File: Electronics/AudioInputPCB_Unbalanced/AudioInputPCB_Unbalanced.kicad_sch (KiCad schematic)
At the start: 109 parts, among them J1 IDC Header, J2 RCA x2, J3 RCA x2, J4 RCA x2, J5 RCA x2, U1 NE5532, U2 NE5532, U3 NE5532, U4 NE5532

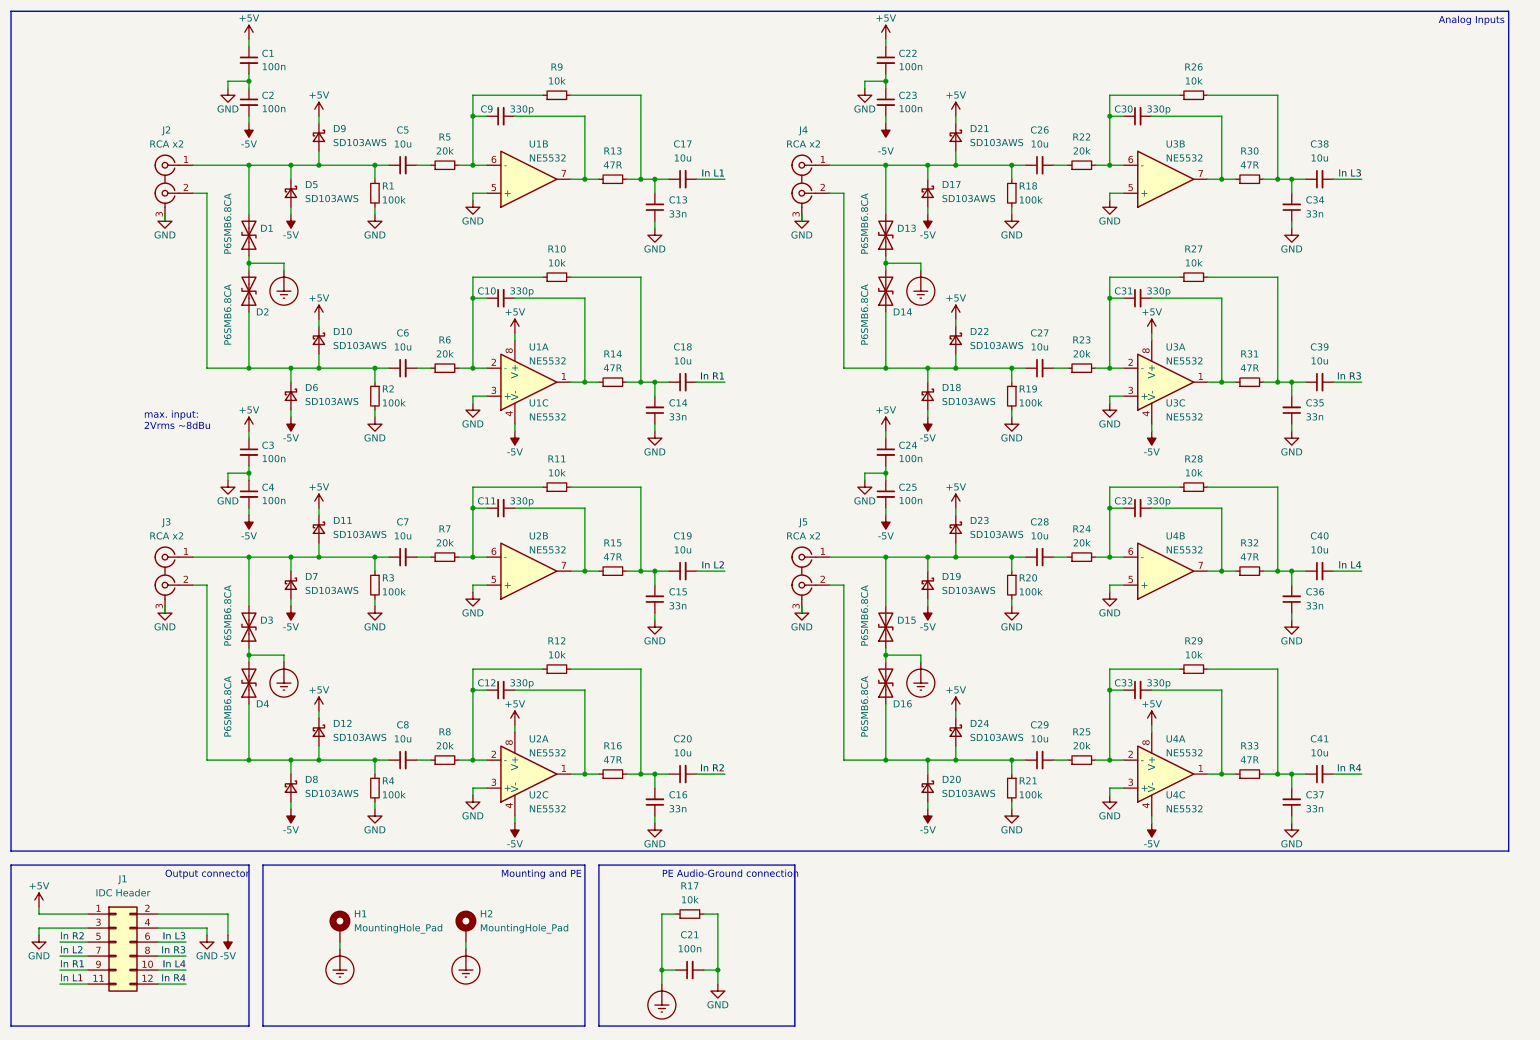
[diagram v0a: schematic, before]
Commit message: Finishes SmallDSP Maxi plus the fitting In- and Output Boards
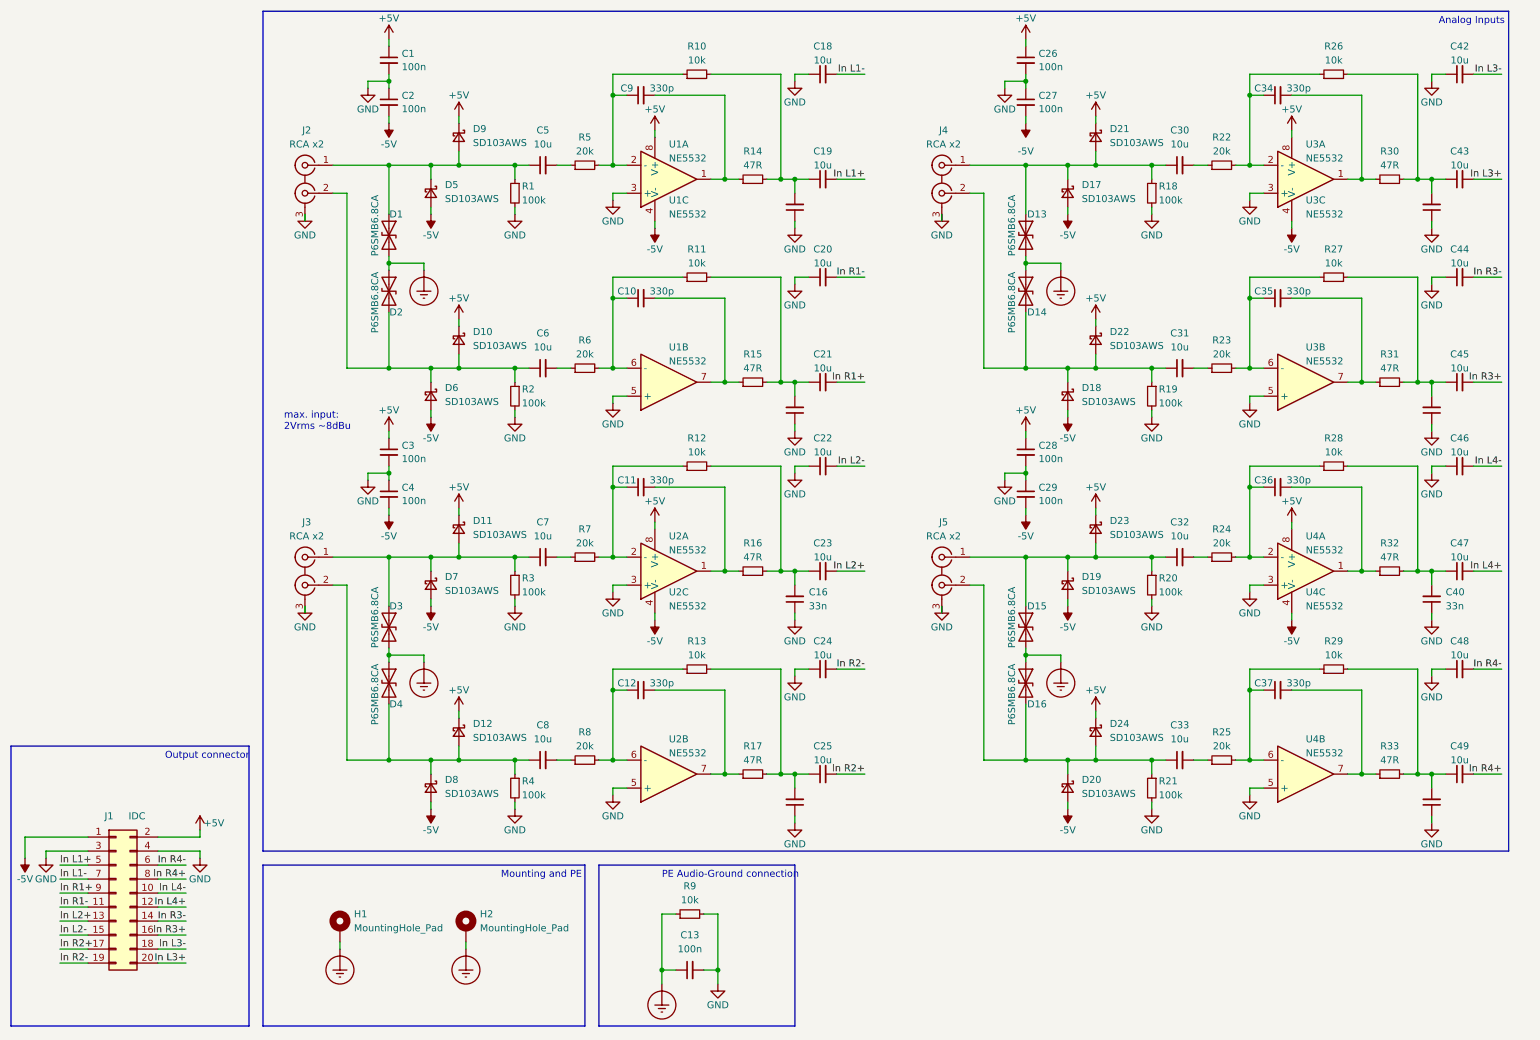
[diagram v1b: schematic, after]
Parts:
- removed C17, C38, C39, C40, C41: 10u, Capacitor_SMD:C_1206_3216Metric, symbol Device:C_Small
- removed J1: IDC Header, Connector_IDC:IDC-Header_2x06_P2.54mm_Vertical, symbol Connector_Generic:Conn_02x06_Odd_Even
- added C21, C22, C23, C24, C25, C42, C43, C44, C45, C46, C47, C48, C49: 10u, Capacitor_SMD:C_1206_3216Metric, symbol Device:C_Small
- added J1: IDC, Connector_IDC:IDC-Header_2x10_P2.54mm_Vertical, symbol Connector_Generic:Conn_02x10_Odd_Even
- renumbered C9 to C10, C12 to C11, C11 to C12, C21 to C13, C13 to C15, C15 to C17, C22 to C26, C23 to C27, C24 to C28, C25 to C29, C27 to C30, C26 to C31, C29 to C32, C28 to C33, C31 to C34, C30 to C35, C33 to C36, C32 to C37, C35 to C38, C34 to C39, C37 to C40, C36 to C41, C6 to C5, C5 to C6, C8 to C7, C7 to C8, C10 to C9, D2 to D1, D9 to D10, D12 to D11, D11 to D12, D14 to D13, D13 to D14, D16 to D15, D15 to D16, D18 to D17, D17 to D18, D20 to D19, D1 to D2, D19 to D20, D22 to D21, D21 to D22, D24 to D23, D23 to D24, D4 to D3, D3 to D4, D6 to D5, D5 to D6, D8 to D7, D7 to D8, D10 to D9, R2 to R1, R9 to R11, R11 to R13, R13 to R15, R15 to R17, R19 to R18, R18 to R19, R1 to R2, R21 to R20, R20 to R21, R23 to R22, R22 to R23, R25 to R24, R24 to R25, R27 to R26, R26 to R27, R29 to R28, R28 to R29, R4 to R3, R31 to R30, R30 to R31, R33 to R32, R32 to R33, R3 to R4, R6 to R5, R5 to R6, R8 to R7, R7 to R8, R17 to R9
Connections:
- net +5V: now also J1.2 (Pin_2)
- net -5V: now also J1.1 (Pin_1)
- net GND: now also C18.1, C20.1, C22.1, C24.1, C42.1, C44.1, C46.1, C48.1, J1.3 (Pin_3), J1.4 (Pin_4)
- net at C30.1, D13.1 (A1), D17.1 (K)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: now also J4.1 (IN1); no longer J4.2 (IN2)
- net at C8.1, D12.2 (A), D4.2 (A2)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: now also J3.2 (IN2); no longer J3.1 (IN1)
- net at C7.1, D11.2 (A), D3.1 (A1)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: now also J3.1 (IN1); no longer J3.2 (IN2)
- net at C17.2, R13.2, R17.2: now also C25.1; no longer C19.1
- net at C38.2, R26.2, R30.2: now also C43.1
- net at C6.1, D10.2 (A), D2.2 (A2)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: now also J2.2 (IN2); no longer J2.1 (IN1)
- net at C5.1, D1.1 (A1), D5.1 (K)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: now also J2.1 (IN1); no longer J2.2 (IN2)
- net at C15.2, R11.2, R15.2: now also C21.1
- net at C32.1, D15.1 (A1), D19.1 (K)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: now also J5.1 (IN1); no longer J5.2 (IN2)
- net at C33.1, D16.2 (A2), D20.1 (K)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: now also J5.2 (IN2); no longer J5.1 (IN1)
- net at C31.1, D14.2 (A2), D18.1 (K)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: now also J4.2 (IN2); no longer J4.1 (IN1)
- net at C39.2, R27.2, R31.2: now also C45.1
- net at C41.2, R29.2, R33.2: now also C49.1
- net at C16.2, R12.2, R16.2: now also C23.1; no longer C20.1
- net at C14.2, R10.2, R14.2: now also C19.1; no longer C18.1
- net at C40.2, R28.2, R32.2: now also C47.1
- net In L2 renamed In L1+
- net In L1+: now also J1.5 (Pin_5)
- net In R1 renamed In L1-
- net In L1-: now also J1.7 (Pin_7)
- net In R2 renamed In R1-
- net In R1-: now also J1.11 (Pin_11)
- new net In L2+: C23.2, J1.13 (Pin_13)
- new net In L2-: C22.2, J1.15 (Pin_15)
- new net In L3+: C43.2, J1.20 (Pin_20)
- new net In L3-: C42.2, J1.18 (Pin_18)
- new net In L4+: C47.2, J1.12 (Pin_12)
- new net In L4-: C46.2, J1.10 (Pin_10)
- new net In R1+: C21.2, J1.9 (Pin_9)
- new net In R2+: C25.2, J1.17 (Pin_17)
- new net In R2-: C24.2, J1.19 (Pin_19)
- new net In R3+: C45.2, J1.16 (Pin_16)
- new net In R3-: C44.2, J1.14 (Pin_14)
- new net In R4+: C49.2, J1.8 (Pin_8)
- new net In R4-: C48.2, J1.6 (Pin_6)
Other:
- moved on the sheet: C1, C10, C11, C12, C16, C2, C26, C27, C28, C29, C3, C30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

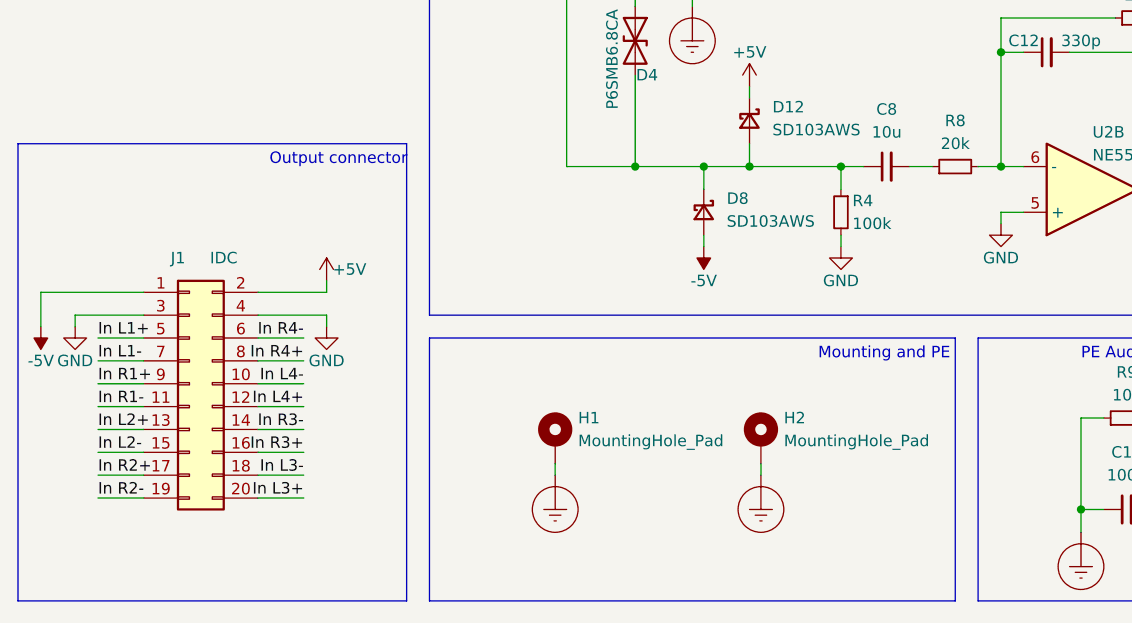
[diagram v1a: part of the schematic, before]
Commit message: adds usb to i2s bridge to micro. Adds tweaks for layout of maxi.
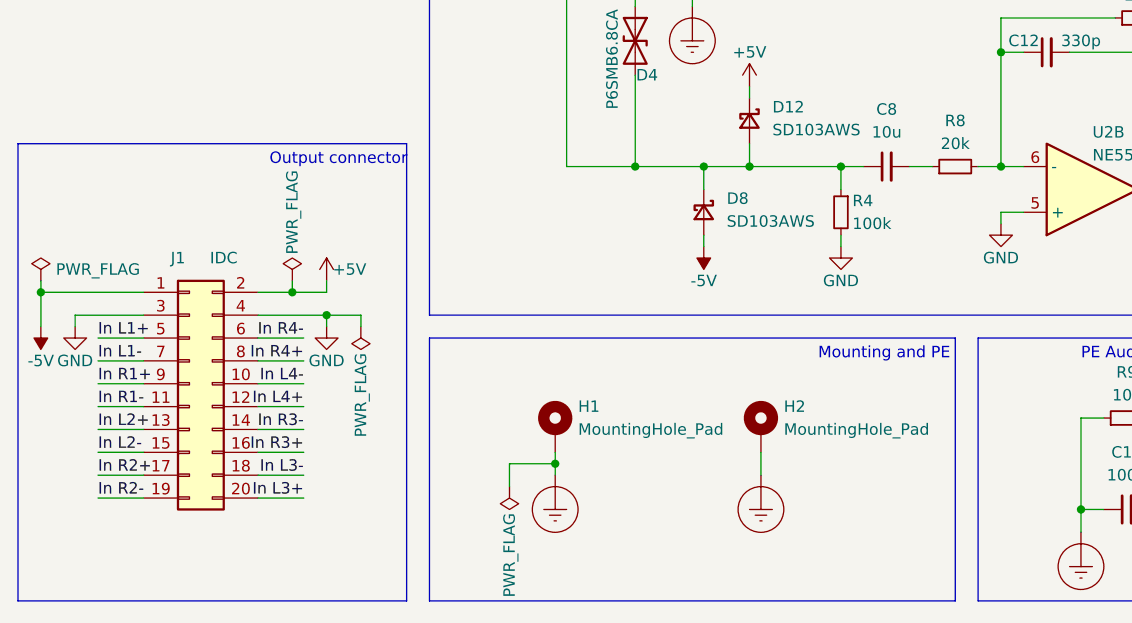
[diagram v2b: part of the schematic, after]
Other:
- moved on the sheet: H1, H2
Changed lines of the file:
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@@
   (title_block
     (title "Unbalanced Analog Input Board for SmallDSP")
-    (date "2023-10-23")
+    (date "2023-11-06")
     (rev "1.0")
     (company "Till Heuer")
@@
   (junction (at 81.28 111.76) (diameter 0) (color 0 0 0 0)
   )
+  (junction (at 15.24 162.56) (diameter 0) (color 0 0 0 0)
+  )
   (junction (at 142.24 151.13) (diameter 0) (color 0 0 0 0)
   )
@@
   (junction (at 237.49 77.47) (diameter 0) (color 0 0 0 0)
   )
+  (junction (at 46.99 165.1) (diameter 0) (color 0 0 0 0)
+  )
   (junction (at 204.47 111.76) (diameter 0) (color 0 0 0 0)
   )
   (junction (at 257.81 151.13) (diameter 0) (color 0 0 0 0)
   )
+  (junction (at 72.39 181.61) (diameter 0) (color 0 0 0 0)
+  )
   (junction (at 81.28 25.4) (diameter 0) (color 0 0 0 0)
   )
@@
   (junction (at 219.71 148.59) (diameter 0) (color 0 0 0 0)
   )
+  (junction (at 43.18 162.56) (diameter 0) (color 0 0 0 0)
+  )
   (junction (at 196.85 40.64) (diameter 0) (color 0 0 0 0)
   )
@@
     (stroke (width 0) (type default))
   )
+  (wire (pts (xy 43.18 162.56) (xy 46.99 162.56))
+    (stroke (width 0) (type default))
+  )
   (wire (pts (xy 152.4 80.01) (xy 149.86 80.01))
     (stroke (width 0) (type default))
@@
     (stroke (width 0) (type default))
   )
+  (wire (pts (xy 67.31 181.61) (xy 72.39 181.61))
+    (stroke (width 0) (type default))
+  )
   (polyline (pts (xy 116.84 167.64) (xy 116.84 196.85))
     (stroke (width 0) (type default))
@@
     (stroke (width 0) (type default))
   )
+  (wire (pts (xy 15.24 161.29) (xy 15.24 162.56))
+    (stroke (width 0) (type default))
+  )
   (wire (pts (xy 257.81 43.18) (xy 255.27 43.18))
     (stroke (width 0) (type default))
@@
     (stroke (width 0) (type default))
   )
+  (wire (pts (xy 72.39 180.34) (xy 72.39 181.61))
+    (stroke (width 0) (type default))
+  )
   (wire (pts (xy 154.94 80.01) (xy 152.4 80.01))
     (stroke (width 0) (type default))
@@
     (stroke (width 0) (type default))
   )
-  (wire (pts (xy 95.25 181.61) (xy 95.25 182.88))
+  (wire (pts (xy 95.25 180.34) (xy 95.25 182.88))
     (stroke (width 0) (type default))
   )
@@
     (stroke (width 0) (type default))
   )
+  (wire (pts (xy 50.8 166.37) (xy 50.8 165.1))
+    (stroke (width 0) (type default))
+  )
   (wire (pts (xy 119.38 111.76) (xy 121.92 111.76))
     (stroke (width 0) (type default))
@@
     (stroke (width 0) (type default))
   )
+  (wire (pts (xy 50.8 165.1) (xy 46.99 165.1))
+    (stroke (width 0) (type default))
+  )
   (wire (pts (xy 154.94 50.8) (xy 154.94 52.07))
     (stroke (width 0) (type default))
@@
     (stroke (width 0) (type default))
   )
-  (wire (pts (xy 39.37 162.56) (xy 46.99 162.56))
+  (wire (pts (xy 39.37 162.56) (xy 43.18 162.56))
     (stroke (width 0) (type default))
   )
@@
     (stroke (width 0) (type default))
   )
+  (wire (pts (xy 43.18 161.29) (xy 43.18 162.56))
+    (stroke (width 0) (type default))
+  )
   (wire (pts (xy 245.11 135.89) (xy 257.81 135.89))
     (stroke (width 0) (type default))
@@
     (stroke (width 0) (type default))
   )
+  (wire (pts (xy 67.31 184.15) (xy 67.31 181.61))
+    (stroke (width 0) (type default))
+  )
   (wire (pts (xy 88.9 85.09) (xy 88.9 86.36))
     (stroke (width 0) (type default))
@@
     )
   )
-  (symbol (lib_id "Mechanical:MountingHole_Pad") (at 72.39 179.07 0) (unit 1)
+  (symbol (lib_id "Mechanical:MountingHole_Pad") (at 72.39 177.8 0) (unit 1)
     (in_bom yes) (on_board yes) (dnp no) (fields_autoplaced)
-    (property "Reference" "H1" (at 74.93 176.5299 0)
+    (property "Reference" "H1" (at 74.93 175.2599 0)
       (effects (font (size 1.27 1.27)) (justify left))
     )
-    (property "Value" "MountingHole_Pad" (at 74.93 179.0699 0)
+    (property "Value" "MountingHole_Pad" (at 74.93 177.7999 0)
       (effects (font (size 1.27 1.27)) (justify left))
     )
-    (property "Footprint" "MountingHole:MountingHole_3.2mm_M3_Pad_Via" (at 72.39 179.07 0)
+    (property "Footprint" "MountingHole:MountingHole_3.2mm_M3_Pad_Via" (at 72.39 177.8 0)
       (effects (font (size 1.27 1.27)) hide)
     )
-    (property "Datasheet" "~" (at 72.39 179.07 0)
+    (property "Datasheet" "~" (at 72.39 177.8 0)
       (effects (font (size 1.27 1.27)) hide)
     )
-    (property "Manufacturer" "-" (at 72.39 179.07 0)
+    (property "Manufacturer" "-" (at 72.39 177.8 0)
       (effects (font (size 1.27 1.27)) hide)
     )
-    (property "Part Number" "-" (at 72.39 179.07 0)
+    (property "Part Number" "-" (at 72.39 177.8 0)
       (effects (font (size 1.27 1.27)) hide)
     )
-    (property "LCSC Part #" "-" (at 72.39 179.07 0)
+    (property "LCSC Part #" "-" (at 72.39 177.8 0)
       (effects (font (size 1.27 1.27)) hide)
     )
@@
     )
   )
+  (symbol (lib_id "power:PWR_FLAG") (at 43.18 161.29 0) (unit 1)
+    (in_bom yes) (on_board yes) (dnp no)
+    (property "Reference" "#FLG02" (at 43.18 159.385 0)
+      (effects (font (size 1.27 1.27)) hide)
+    )
+    (property "Value" "PWR_FLAG" (at 43.18 153.67 90)
+      (effects (font (size 1.27 1.27)))
+    )
+    (property "Footprint" "" (at 43.18 161.29 0)
+      (effects (font (size 1.27 1.27)) hide)
+    )
+    (property "Datasheet" "~" (at 43.18 161.29 0)
+      (effects (font (size 1.27 1.27)) hide)
+    )
+    (pin "1")
+    (instances
+      (project "AudioInputPCB_Unbalanced"
+        (path "/17188c6f-f81f-4113-81fa-be4890d4152c"
+          (reference "#FLG02") (unit 1)
+        )
+      )
+    )
+  )
   (symbol (lib_id "power:GND") (at 193.04 97.79 0) (unit 1)
     (in_bom yes) (on_board yes) (dnp no)
@@
     )
   )
+  (symbol (lib_id "power:PWR_FLAG") (at 15.24 161.29 0) (unit 1)
+    (in_bom yes) (on_board yes) (dnp no)
+    (property "Reference" "#FLG01" (at 15.24 159.385 0)
+      (effects (font (size 1.27 1.27)) hide)
+    )
+    (property "Value" "PWR_FLAG" (at 21.59 160.02 0)
+      (effects (font (size 1.27 1.27)))
+    )
+    (property "Footprint" "" (at 15.24 161.29 0)
+      (effects (font (size 1.27 1.27)) hide)
+    )
+    (property "Datasheet" "~" (at 15.24 161.29 0)
+      (effects (font (size 1.27 1.27)) hide)
+    )
+    (pin "1")
+    (instances
+      (project "AudioInputPCB_Unbalanced"
+        (path "/17188c6f-f81f-4113-81fa-be4890d4152c"
+          (reference "#FLG01") (unit 1)
+        )
+      )
+    )
+  )
   (symbol (lib_id "Connector:Conn_Coaxial_x2") (at 181.61 114.3 0) (mirror y) (unit 1)
     (in_bom yes) (on_board yes) (dnp no)
@@
     )
   )
+  (symbol (lib_id "power:PWR_FLAG") (at 50.8 166.37 180) (unit 1)
+    (in_bom yes) (on_board yes) (dnp no)
+    (property "Reference" "#FLG03" (at 50.8 168.275 0)
+      (effects (font (size 1.27 1.27)) hide)
+    )
+    (property "Value" "PWR_FLAG" (at 50.8 173.99 90)
+      (effects (font (size 1.27 1.27)))
+    )
+    (property "Footprint" "" (at 50.8 166.37 0)
+      (effects (font (size 1.27 1.27)) hide)
+    )
+    (property "Datasheet" "~" (at 50.8 166.37 0)
+      (effects (font (size 1.27 1.27)) hide)
+    )
+    (pin "1")
+    (instances
+      (project "AudioInputPCB_Unbalanced"
+        (path "/17188c6f-f81f-4113-81fa-be4890d4152c"
+          (reference "#FLG03") (unit 1)
+        )
+      )
+    )
+  )
   (symbol (lib_id "power:GND") (at 140.97 189.23 0) (unit 1)
     (in_bom yes) (on_board yes) (dnp no)
@@
     )
   )
-  (symbol (lib_id "Mechanical:MountingHole_Pad") (at 95.25 179.07 0) (unit 1)
+  (symbol (lib_id "Mechanical:MountingHole_Pad") (at 95.25 177.8 0) (unit 1)
     (in_bom yes) (on_board yes) (dnp no) (fields_autoplaced)
-    (property "Reference" "H2" (at 97.79 176.5299 0)
+    (property "Reference" "H2" (at 97.79 175.2599 0)
       (effects (font (size 1.27 1.27)) (justify left))
     )
-    (property "Value" "MountingHole_Pad" (at 97.79 179.0699 0)
+    (property "Value" "MountingHole_Pad" (at 97.79 177.7999 0)
       (effects (font (size 1.27 1.27)) (justify left))
     )
-    (property "Footprint" "MountingHole:MountingHole_3.2mm_M3_Pad_Via" (at 95.25 179.07 0)
+    (property "Footprint" "MountingHole:MountingHole_3.2mm_M3_Pad_Via" (at 95.25 177.8 0)
       (effects (font (size 1.27 1.27)) hide)
     )
-    (property "Datasheet" "~" (at 95.25 179.07 0)
+    (property "Datasheet" "~" (at 95.25 177.8 0)
       (effects (font (size 1.27 1.27)) hide)
     )
-    (property "Manufacturer" "-" (at 95.25 179.07 0)
+    (property "Manufacturer" "-" (at 95.25 177.8 0)
       (effects (font (size 1.27 1.27)) hide)
     )
-    (property "Part Number" "-" (at 95.25 179.07 0)
+    (property "Part Number" "-" (at 95.25 177.8 0)
       (effects (font (size 1.27 1.27)) hide)
     )
-    (property "LCSC Part #" "-" (at 95.25 179.07 0)
+    (property "LCSC Part #" "-" (at 95.25 177.8 0)
       (effects (font (size 1.27 1.27)) hide)
     )
@@
         )
       )
+    )
+  )
+  (symbol (lib_id "power:PWR_FLAG") (at 67.31 184.15 180) (unit 1)
+    (in_bom yes) (on_board yes) (dnp no)
+    (property "Reference" "#FLG04" (at 67.31 186.055 0)
+      (effects (font (size 1.27 1.27)) hide)
+    )
+    (property "Value" "PWR_FLAG" (at 67.31 191.77 90)
+      (effects (font (size 1.27 1.27)))
+    )
+    (property "Footprint" "" (at 67.31 184.15 0)
+      (effects (font (size 1.27 1.27)) hide)
+    )
+    (property "Datasheet" "~" (at 67.31 184.15 0)
+      (effects (font (size 1.27 1.27)) hide)
+    )
+    (pin "1")
+    (instances
+      (project "AudioInputPCB_Unbalanced"
+        (path "/17188c6f-f81f-4113-81fa-be4890d4152c"
+          (reference "#FLG04") (unit 1)
+        )
+      )

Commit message: Adds final state of Maxi rev 1.0 and unbalanced IO boards rev 1.0.
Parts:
- D1, D13, D14, D15, D16, D2, D3, D4: value P6SMB6.8CA -> H5VL10B; footprint Diode_SMD:D_SMB -> 1_Project_Footprints:DFN1006-2; LCSC Part # C78395 -> C7420372; Manufacturer Brightking -> hongjiacheng; Part Number P6SMB6.8CA/TR13 -> H5VL10B
